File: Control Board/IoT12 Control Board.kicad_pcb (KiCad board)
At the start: 2 copper layers, 99.1 x 69.8 mm, 114 parts, among them J10 USB_B_Micro, J11 Conn_ARM_JTAG_SWD_10, J9 Conn_ARM_JTAG_SWD_10, Q1 MMBT2222, Q2 MMBT2222, Q3 AOD403, SW1 Rotary encoder EC11 Plum 15mm, SW2 SW_Push, U1 ATSAMD21G18A-AU, U2 ADS1115IDGS, U3 INA826AID, U4 INA826AID, U5 LM2596S-ADJ, U6 AT24C32, U7 MAX809S, Y1 32768Hz

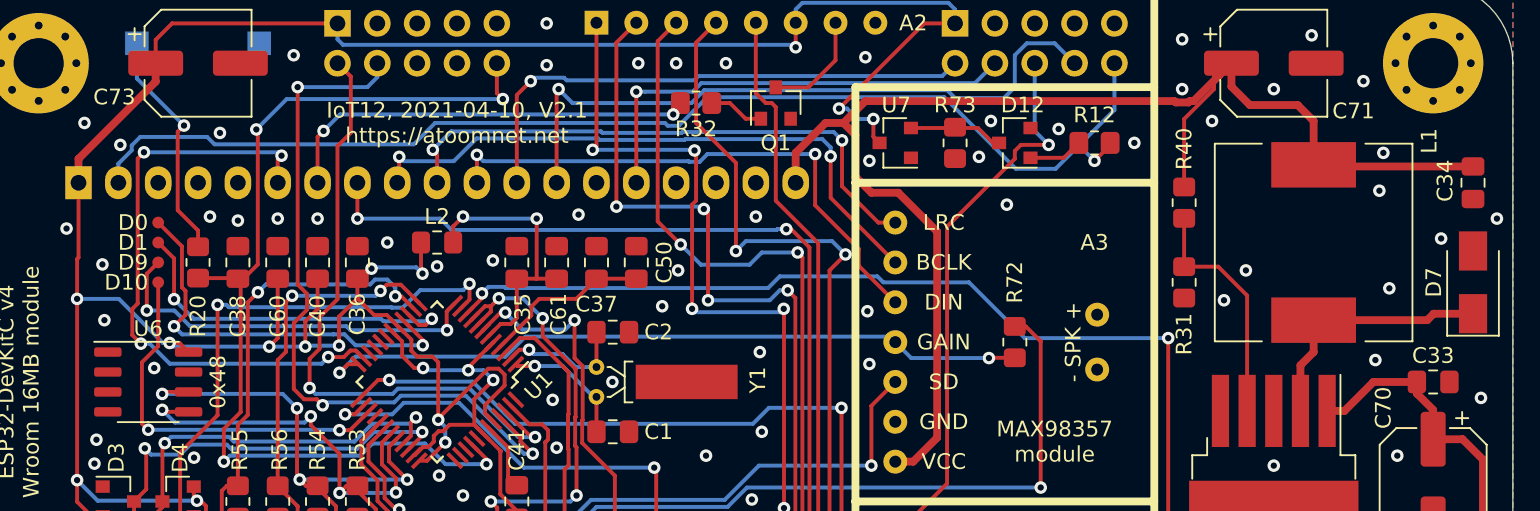
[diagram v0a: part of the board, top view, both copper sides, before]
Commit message: Changed some footprints to that have 3d models.
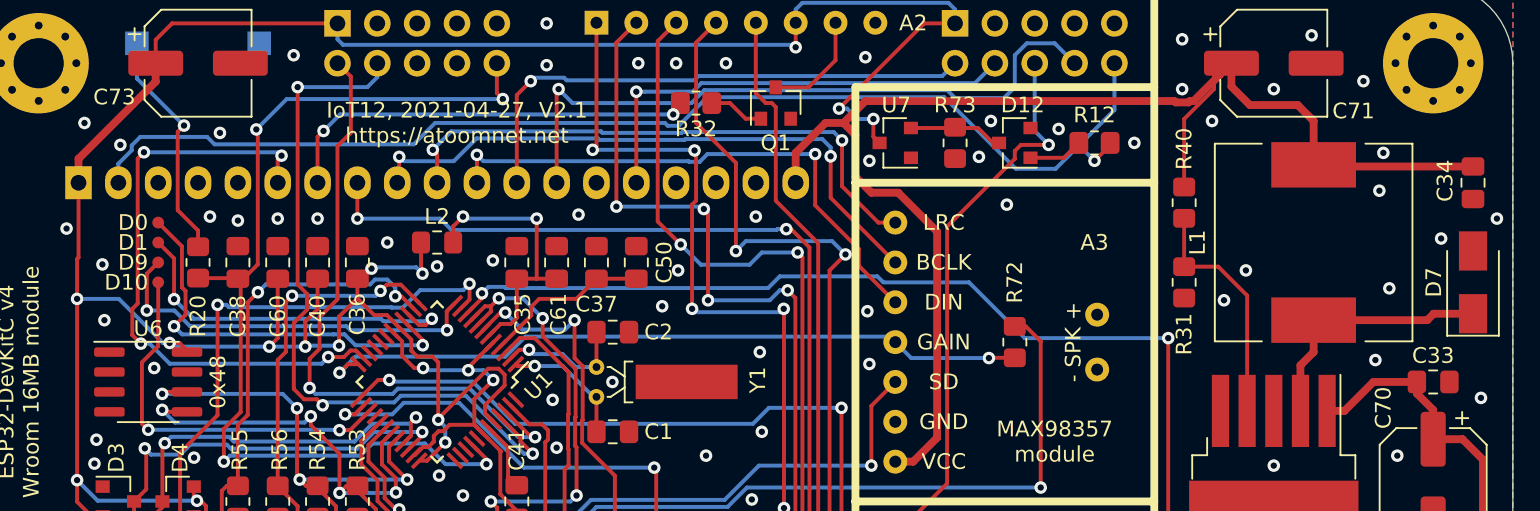
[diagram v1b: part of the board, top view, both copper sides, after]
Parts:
- L1: footprint Inductor_SMD:L_12x12mm_H8mm -> Inductor-fixed:L_12x12mm_H8mm
- U6: footprint Package_SO:SO-8_3.9x4.9mm_P1.27mm -> Package_SO:SOIC-8_3.9x4.9mm_P1.27mm
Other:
- board text added: "IoT12, 2021-04-27, V2.1 https://atoomnet.net"
- board text removed: "IoT12, 2021-04-10, V2.1 https://atoomnet.net"

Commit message: Changed usb connector to one that has a 3d model.
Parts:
- J10: footprint Connector_USB:USB_Micro-B_Amphenol_10118194_Horizontal -> Connector_USB-fixed:USB_Micro-B_Amphenol_10118194_Horizontal
